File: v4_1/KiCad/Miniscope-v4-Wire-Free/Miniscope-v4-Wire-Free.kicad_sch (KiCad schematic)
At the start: 114 parts, among them J1 0475710001, J10 Conn_01x01, J11 Conn_01x01, J12 Conn_01x01, J14 Conn_01x01, J15 Conn_01x01, J16 Conn_01x01, J17 Conn_01x01, J18 Conn_01x01, J19 Conn_01x01, J2 Conn_01x04, J20 Conn_01x01, J21 Conn_01x01, J22 Conn_01x01, J23 Conn_01x01, J24 Conn_01x01, J25 Conn_01x01, J26 Conn_01x01, J27 Conn_01x01, J3 Conn_01x04, J4 Conn_01x01, J5 Conn_01x01, J6 Conn_01x01, J7 Conn_01x01, J8 Conn_01x01, J9 Conn_01x01, Q1 NTK3134NT1G, Q2 MMBT3904LP-7B, SW1 TL3780AF330QG, U1 LTC3554, U2 HV892, U3 LTC3218, U4 MAX13030EETE+BGA, U5 TSOP57438TT1, U6 ATSAMD51J20A-UUT-EFP, U7 NCP163AMX330TBG, U8 NOIP1SN0480A, U9 LMV321IDCKR, Y2 Crystal

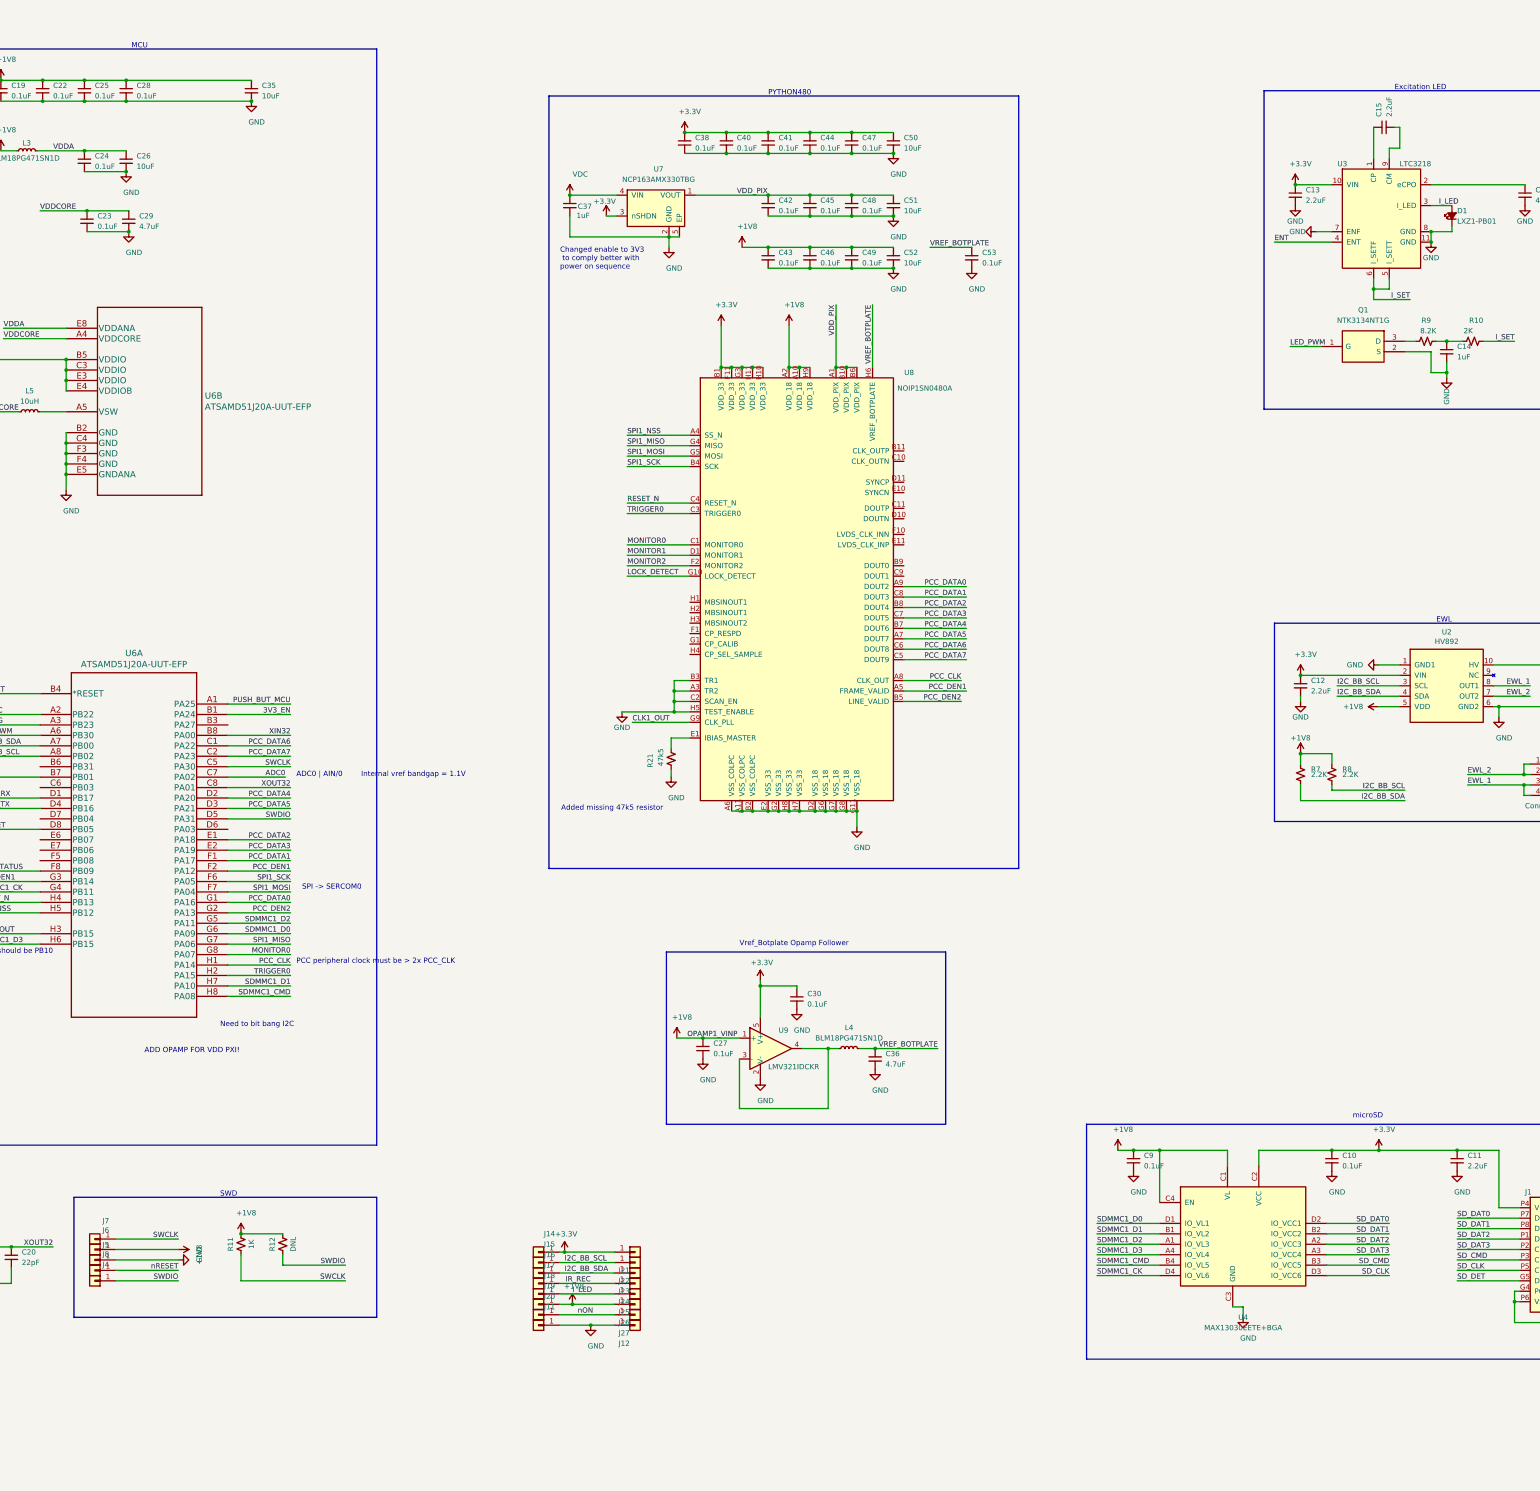
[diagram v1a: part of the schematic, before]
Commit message: Updates to the project
- Added code to test the functionality of the v4 WF and validate the design
- Fixed a bug that left the EWL run continuously even if it was not recording. Now once the recording ends the EWL goes to sleep mode
- Modified the threshold for which the recording stops once the battery ADC reading reaches certain value
- Fixed a typo on the jupyter notebook name
- Fixed the programming cable by changing the target programming pins footprint
- Added a folder with a KiCAD project for the EWL cable
- For both things I generated new gerbers, which I checked using the gerber viewer
- Not uploaded to the repo due to size constrains: videos demonstrating that the Miniscope can record continuously for over 20 minutes

To do (in the short term):

- Add requirements to create a conda environment for easier use of the DAQ notebook
- Clean a bit more the code
- Add to the documentation the fix we applied to fix the bug that prevented the Miniscope to not run on Release mode
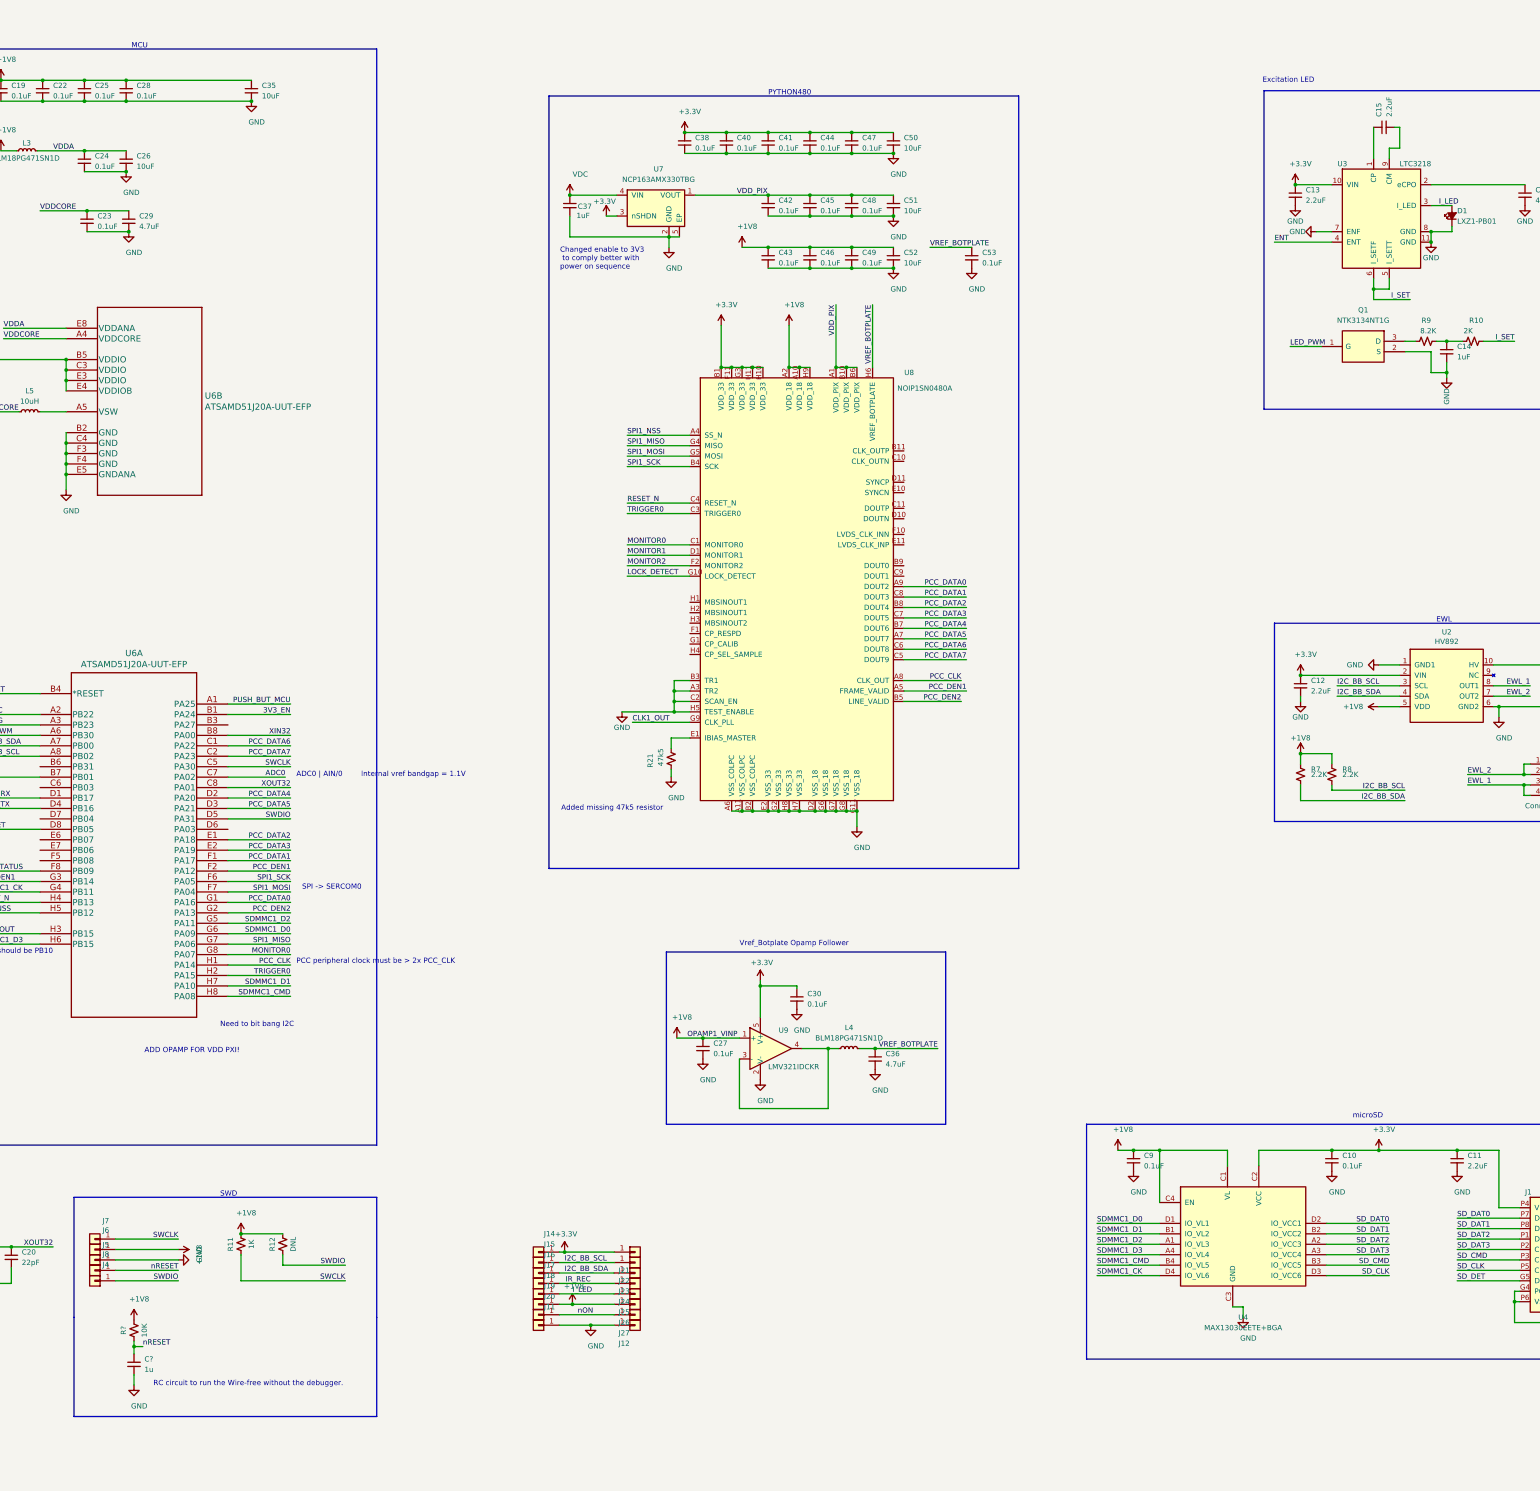
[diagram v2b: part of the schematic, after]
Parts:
- added C?: 1u, .Capacitor:C_0201_0603Metric_L, symbol .Device:C_Small
- added R?: 10K, .Resistor:R_0201_0603Metric_ERJ_L, symbol .Device:R_Small_US
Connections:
- net +1V8: now also R?.1
- net GND: now also C?.2
- net nRESET: now also C?.1, R?.2
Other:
- note added: "RC circuit to run the Wire-free without the debugger."
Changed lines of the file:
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@@
   (junction (at 80.01 74.93) (diameter 0) (color 0 0 0 0)
   )
+  (junction (at 203.835 341.122) (diameter 0) (color 0 0 0 0)
+  )
   (junction (at 539.75 330.2) (diameter 0) (color 0 0 0 0)
   )
@@
     (stroke (width 0) (type default) (color 0 0 0 0))
   )
+  (polyline (pts (xy 262.89 358.14) (xy 189.23 358.14))
+    (stroke (width 0) (type default) (color 0 0 0 0))
+  )
   (wire (pts (xy 173.99 325.755) (xy 173.99 321.945))
     (stroke (width 0) (type default) (color 0 0 0 0))
@@
     (stroke (width 0) (type default) (color 0 0 0 0))
   )
+  (polyline (pts (xy 262.89 334.01) (xy 262.89 358.14))
+    (stroke (width 0) (type default) (color 0 0 0 0))
+  )
   (wire (pts (xy 334.5434 200.66) (xy 334.5434 202.5142))
     (stroke (width 0) (type default) (color 0 0 0 0))
@@
     (stroke (width 0) (type default) (color 0 0 0 0))
   )
-  (polyline (pts (xy 262.89 334.01) (xy 189.23 334.01))
-    (stroke (width 0) (type default) (color 0 0 0 0))
-  )
   (wire (pts (xy 532.13 96.52) (xy 539.75 96.52))
     (stroke (width 0) (type default) (color 0 0 0 0))
@@
     (stroke (width 0) (type default) (color 0 0 0 0))
   )
+  (wire (pts (xy 203.835 347.98) (xy 203.835 350.52))
+    (stroke (width 0) (type default) (color 0 0 0 0))
+  )
   (wire (pts (xy 29.21 76.2) (xy 29.21 74.93))
     (stroke (width 0) (type default) (color 0 0 0 0))
   )
+  (wire (pts (xy 203.835 339.725) (xy 203.835 341.122))
+    (stroke (width 0) (type default) (color 0 0 0 0))
+  )
   (wire (pts (xy 339.09 184.15) (xy 335.28 184.15))
     (stroke (width 0) (type default) (color 0 0 0 0))
@@
     (stroke (width 0) (type default) (color 0 0 0 0))
   )
+  (wire (pts (xy 203.835 341.122) (xy 205.994 341.122))
+    (stroke (width 0) (type default) (color 0 0 0 0))
+  )
   (wire (pts (xy 43.18 91.44) (xy 36.83 91.44))
     (stroke (width 0) (type default) (color 0 0 0 0))
@@
     (stroke (width 0) (type default) (color 0 0 0 0))
   )
+  (wire (pts (xy 203.835 341.122) (xy 203.835 342.9))
+    (stroke (width 0) (type default) (color 0 0 0 0))
+  )
   (wire (pts (xy 165.735 243.205) (xy 180.975 243.205))
     (stroke (width 0) (type default) (color 0 0 0 0))
@@
     (stroke (width 0) (type default) (color 0 0 0 0))
   )
+  (polyline (pts (xy 189.23 358.14) (xy 189.23 334.01))
+    (stroke (width 0) (type default) (color 0 0 0 0))
+  )
   (wire (pts (xy 199.39 322.58) (xy 214.63 322.58))
     (stroke (width 0) (type default) (color 0 0 0 0))
@@
     (effects (font (size 1.27 1.27)) (justify left bottom))
   )
-  (text "Excitation LED" (at 510.54 35.56 0)
+  (text "Excitation LED" (at 478.409 33.782 0)
     (effects (font (size 1.27 1.27)) (justify left bottom))
   )
@@
     (effects (font (size 1.27 1.27)) (justify left bottom))
   )
+  (text "RC circuit to run the Wire-free without the debugger."
+    (at 208.534 350.901 0)
+    (effects (font (size 1.27 1.27)) (justify left bottom))
+  )
   (text "PCC peripheral clock must be > 2x PCC_CLK" (at 243.332 248.158 0)
     (effects (font (size 1.27 1.27)) (justify left bottom))
@@
     (effects (font (size 1.27 1.27)) (justify right bottom))
   )
+  (label "nRESET" (at 205.994 341.122 0)
+    (effects (font (size 1.27 1.27)) (justify left bottom))
+  )
   (label "VDDCORE" (at 172.085 95.885 0)
     (effects (font (size 1.27 1.27)) (justify left bottom))
@@
     (pin "1")
   )
+  (symbol (lib_id ".Device:C_Small") (at 203.835 345.44 0) (unit 1)
+    (in_bom yes) (on_board yes)
+    (property "Reference" "C?" (id 0) (at 206.375 344.17 0)
+      (effects (font (size 1.27 1.27)) (justify left))
+    )
+    (property "Value" "1u" (id 1) (at 206.375 346.71 0)
+      (effects (font (size 1.27 1.27)) (justify left))
+    )
+    (property "Footprint" ".Capacitor:C_0201_0603Metric_L" (id 2) (at 203.835 345.44 0)
+      (effects (font (size 1.27 1.27)) hide)
+    )
+    (property "Datasheet" "~" (id 3) (at 203.835 345.44 0)
+      (effects (font (size 1.27 1.27)) hide)
+    )
+    (property "Description" "CAP CER 22PF 50V C0G/NP0 0201" (id 4) (at 203.835 345.44 0)
+      (effects (font (size 1.27 1.27)) hide)
+    )
+    (property "Manufacturer_Name" "Murata" (id 5) (at 203.835 345.44 0)
+      (effects (font (size 1.27 1.27)) hide)
+    )
+    (property "Manufacturer_Part_Number" "GRM0335C1H220GA01D" (id 6) (at 203.835 345.44 0)
+      (effects (font (size 1.27 1.27)) hide)
+    )
+    (pin "1")
+    (pin "2")
+  )
+  (symbol (lib_id "power:GND") (at 203.835 350.52 0) (unit 1)
+    (in_bom yes) (on_board yes)
+    (property "Reference" "#PWR?" (id 0) (at 203.835 356.87 0)
+      (effects (font (size 1.27 1.27)) hide)
+    )
+    (property "Value" "GND" (id 1) (at 205.105 355.6 0))
+    (property "Footprint" "" (id 2) (at 203.835 350.52 0)
+      (effects (font (size 1.27 1.27)) hide)
+    )
+    (property "Datasheet" "" (id 3) (at 203.835 350.52 0)
+      (effects (font (size 1.27 1.27)) hide)
+    )
+    (pin "1")
+  )
+  (symbol (lib_id "power:+1V8") (at 203.835 334.645 0) (unit 1)
+    (in_bom yes) (on_board yes)
+    (property "Reference" "#PWR?" (id 0) (at 203.835 338.455 0)
+      (effects (font (size 1.27 1.27)) hide)
+    )
+    (property "Value" "+1V8" (id 1) (at 205.105 329.565 0))
+    (property "Footprint" "" (id 2) (at 203.835 334.645 0)
+      (effects (font (size 1.27 1.27)) hide)
+    )
+    (property "Datasheet" "" (id 3) (at 203.835 334.645 0)
+      (effects (font (size 1.27 1.27)) hide)
+    )
+    (pin "1")
+  )
+  (symbol (lib_id ".Device:R_Small_US") (at 203.835 337.185 0) (unit 1)
+    (in_bom yes) (on_board yes)
+    (property "Reference" "R?" (id 0) (at 201.295 337.185 90))
+    (property "Value" "10K" (id 1) (at 206.375 337.185 90))
+    (property "Footprint" ".Resistor:R_0201_0603Metric_ERJ_L" (id 2) (at 203.835 337.185 0)
+      (effects (font (size 1.27 1.27)) hide)
+    )
+    (property "Datasheet" "~" (id 3) (at 203.835 337.185 0)
+      (effects (font (size 1.27 1.27)) hide)
+    )
+    (property "Description" "RES SMD 1K OHM 1% 1/20W 0201" (id 4) (at 203.835 337.185 0)
+      (effects (font (size 1.27 1.27)) hide)
+    )
+    (property "Manufacturer_Name" "Vishay Dale" (id 5) (at 203.835 337.185 0)
+      (effects (font (size 1.27 1.27)) hide)
+    )
+    (property "Manufacturer_Part_Number" "CRCW02011K00FKED" (id 6) (at 203.835 337.185 0)
+      (effects (font (size 1.27 1.27)) hide)
+    )
+    (pin "1")
+    (pin "2")
+  )
   (sheet_instances
     (path "/" (page "1"))
@@
       (reference "#PWR0148") (unit 1) (value "+3.3V") (footprint "")
     )
+    (path "/99fa9632-950e-495d-bb41-8aaccf470dca"
+      (reference "#PWR?") (unit 1) (value "GND") (footprint "")
+    )
+    (path "/a035d06a-59fd-4fbe-82f6-0a506f9568d5"
+      (reference "#PWR?") (unit 1) (value "+1V8") (footprint "")
+    )
     (path "/00000000-0000-0000-0000-000060da6e2b"
       (reference "C1") (unit 1) (value "10uF") (footprint ".Capacitor:C_0402_1005Metric_L")
@@
       (reference "C53") (unit 1) (value "0.1uF") (footprint ".Capacitor:C_0201_0603Metric_L")
     )
+    (path "/87f00cd9-90d4-484f-8b44-14f6eea3a247"
+      (reference "C?") (unit 1) (value "1u") (footprint ".Capacitor:C_0201_0603Metric_L")
+    )
     (path "/00000000-0000-0000-0000-0000609f2067"
       (reference "D1") (unit 1) (value "LXZ1-PB01") (footprint ".LED:LED_LXZ1_PR01_L")
@@
       (reference "R21") (unit 1) (value "47k5") (footprint ".Resistor:R_0201_0603Metric_ERJ_L")
     )
+    (path "/e58dd0a0-f7a8-4c7a-8437-b91a27261650"
+      (reference "R?") (unit 1) (value "10K") (footprint ".Resistor:R_0201_0603Metric_ERJ_L")
+    )
     (path "/00000000-0000-0000-0000-000061acacbf"
